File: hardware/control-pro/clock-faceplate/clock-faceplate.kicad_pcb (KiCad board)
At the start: 2 copper layers, 100 x 90 mm, 11 parts

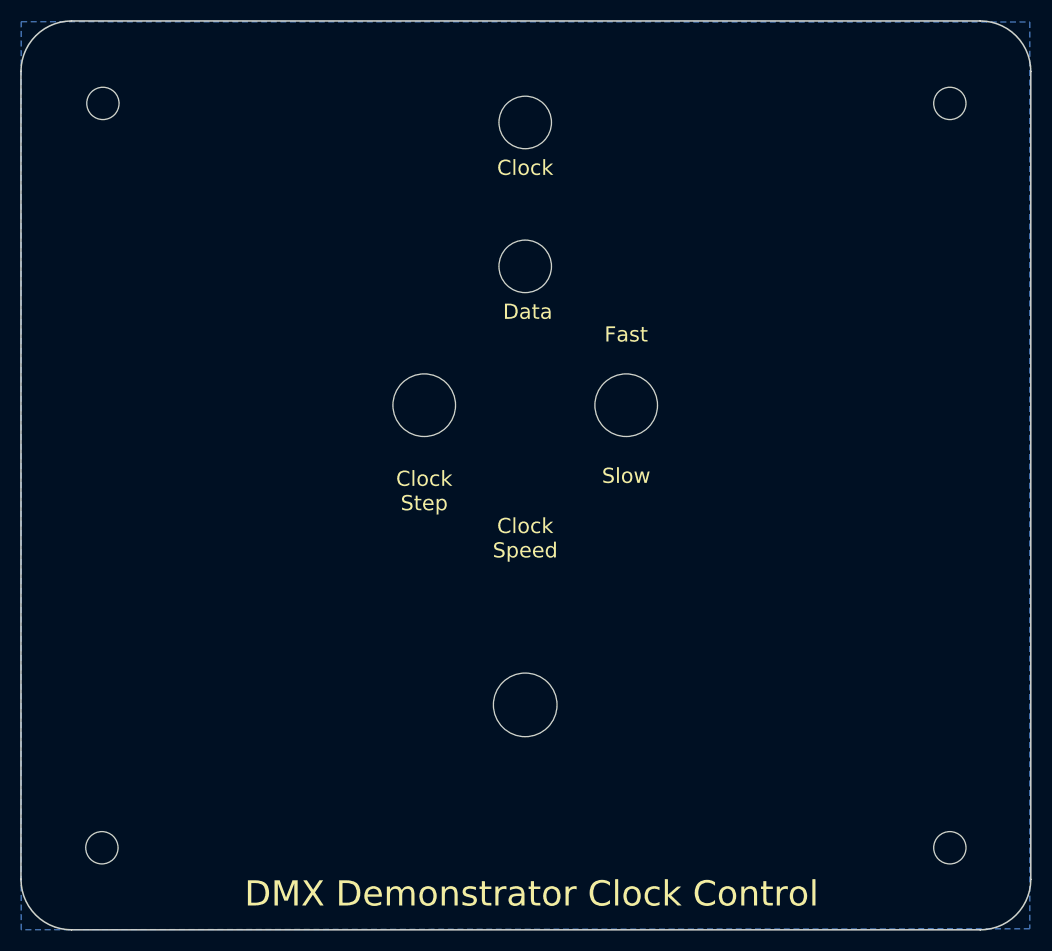
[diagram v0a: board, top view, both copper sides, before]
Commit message: Add copper pours to faceplates.
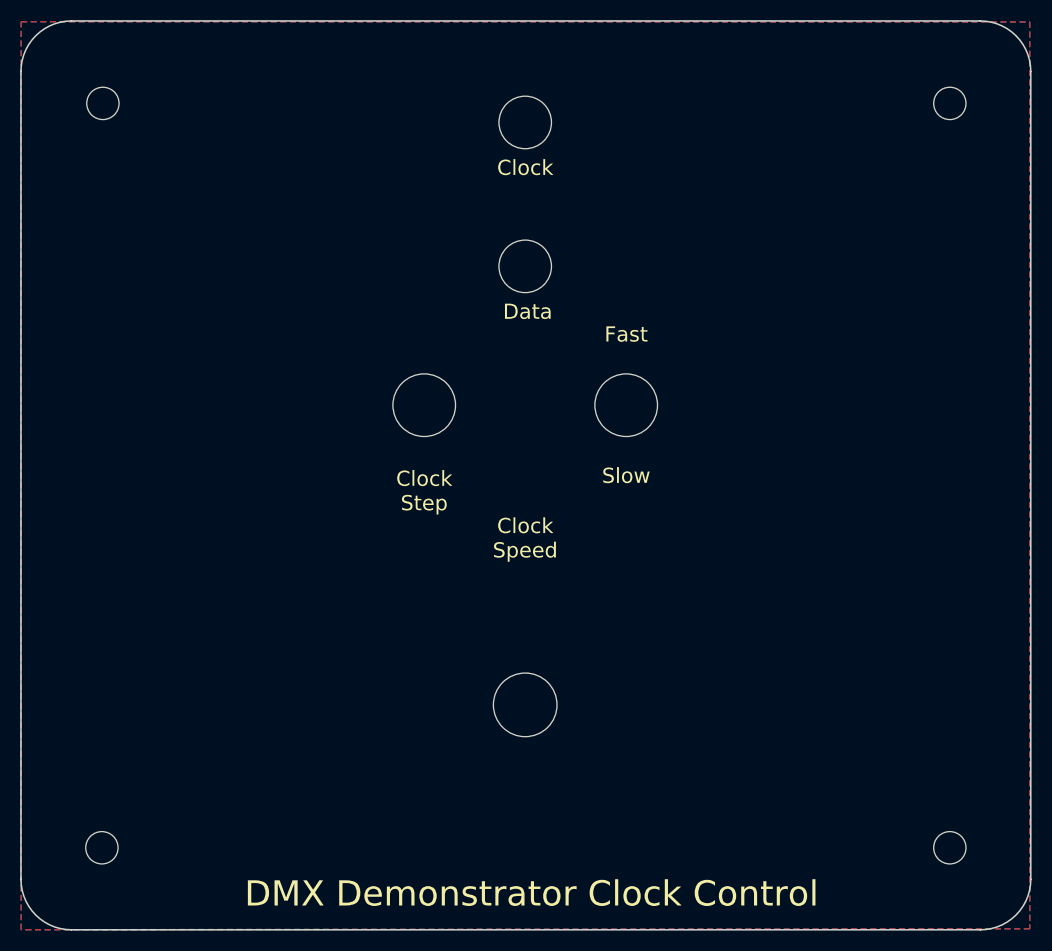
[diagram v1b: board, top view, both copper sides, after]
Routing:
- added copper zone on F.Cu, net GND
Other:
- board text added: "DMX-CPCF, Rev 1.3 Crazy Giraffe Software"
- board text removed: "DMX-CPCF, Rev 1.2 Crazy Giraffe Software"
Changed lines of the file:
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@@
   (title_block
     (title "DMX Demonstrator - Control-Pro Clock (DMX-CPCF)")
-    (date 2023-02-11)
-    (rev 1.2)
+    (date 2023-12-04)
+    (rev 1.3)
     (company "Crazy Giraffe Software")
     (comment 2 "Designed by: SparkyBobo")
@@
     (effects (font (size 1.5 1.5) (thickness 0.3)))
   )
-  (gr_text "DMX-CPCF, Rev 1.2\nCrazy Giraffe Software" (at 160.414 136.102) (layer B.SilkS)
+  (gr_text "DMX-CPCF, Rev 1.3\nCrazy Giraffe Software" (at 160.414 136.102) (layer B.SilkS)
     (effects (font (size 1 1) (thickness 0.15)) (justify mirror))
   )
@@
     (connect_pads (clearance 0.508))
     (min_thickness 0.254)
+    (fill yes (arc_segments 16) (thermal_gap 0.508) (thermal_bridge_width 0.508))
+    (polygon
+      (pts
+        (xy 87.122 48.768) (xy 187.004 48.792) (xy 187.004 138.592) (xy 87.122 138.684)
+      )
+    )
+  )
+  (zone (net 1) (net_name GND) (layer F.Cu) (hatch edge 0.508)
+    (connect_pads (clearance 0.508))
+    (min_thickness 0.254)

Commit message: Update nets for copper pours on control faceplate.
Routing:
- added copper zone on B.Cu, net (none)
- added copper zone on F.Cu, net (none)
- removed copper zone on B.Cu, net GND
- removed copper zone on F.Cu, net GND
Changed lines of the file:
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@@
     (zones 0)
     (modules 11)
-    (nets 2)
+    (nets 1)
   )
   (page A4)
@@
   )
   (net 0 "")
-  (net 1 GND)
   (net_class Default "This is the default net class."
     (clearance 0.2)
@@
   (gr_circle (center 179.088 56.804285) (end 179.85 51.216285) (layer Dwgs.User) (width 0.2))
   (gr_circle (center 95.218 56.856) (end 100.857715 56.856) (layer Dwgs.User) (width 0.2))
-  (zone (net 1) (net_name GND) (layer B.Cu) (hatch edge 0.508)
+  (zone (net 0) (net_name "") (layer B.Cu) (hatch edge 0.508)
     (connect_pads (clearance 0.508))
     (min_thickness 0.254)
@@
     )
   )
-  (zone (net 1) (net_name GND) (layer F.Cu) (hatch edge 0.508)
+  (zone (net 0) (net_name "") (layer F.Cu) (hatch edge 0.508)
     (connect_pads (clearance 0.508))
     (min_thickness 0.254)
